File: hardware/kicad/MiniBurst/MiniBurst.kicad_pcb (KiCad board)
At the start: 2 copper layers, 30 x 113.5 mm, 65 parts, among them J1 TRIG_IN, J2 TRIG_OUT, J3 EXT_CLK, J4 DURATION_OUT, J5 END_OUT, J6 PULSES_OUT, J8 Conn_01x10_Pin, SW1 RETRIG, SW2 STEPS, U1 LM358, U2 40106, U3 4017, U4 LM358, U5 LM358

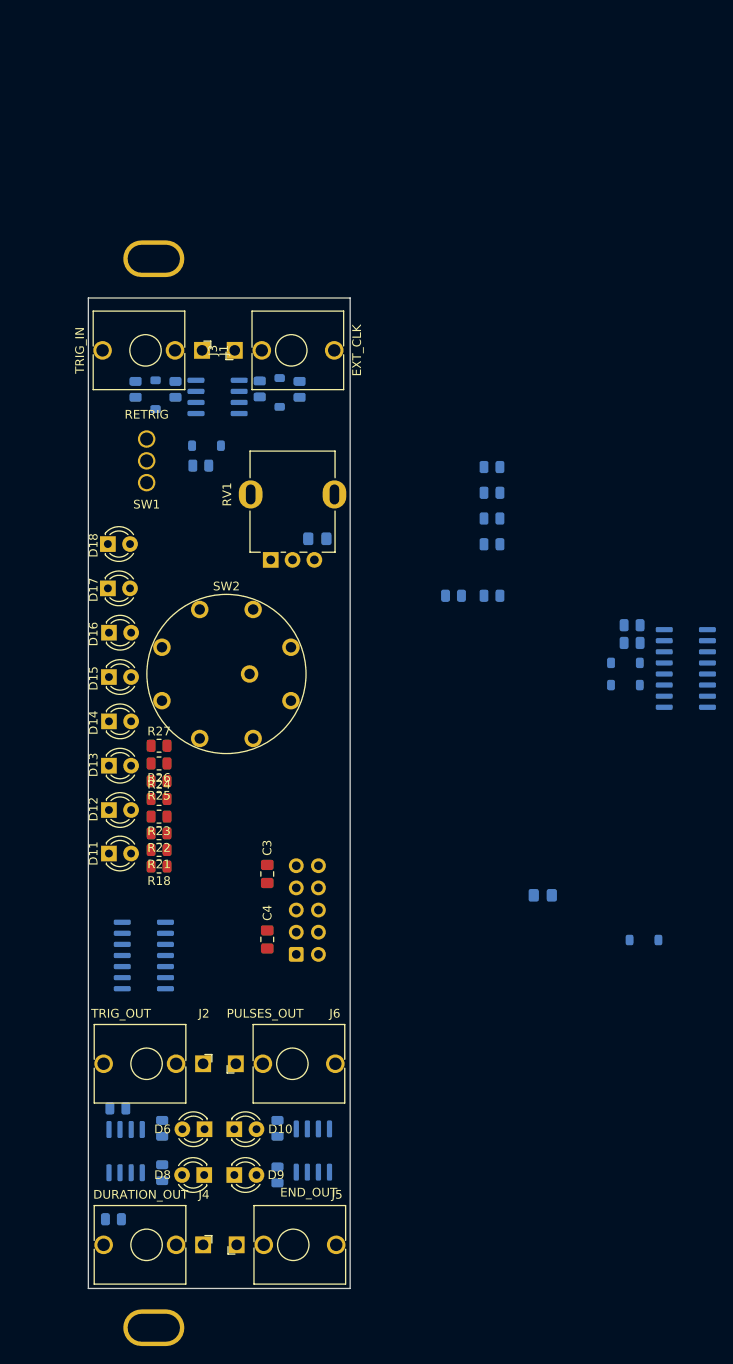
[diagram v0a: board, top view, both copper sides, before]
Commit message: done with panel art
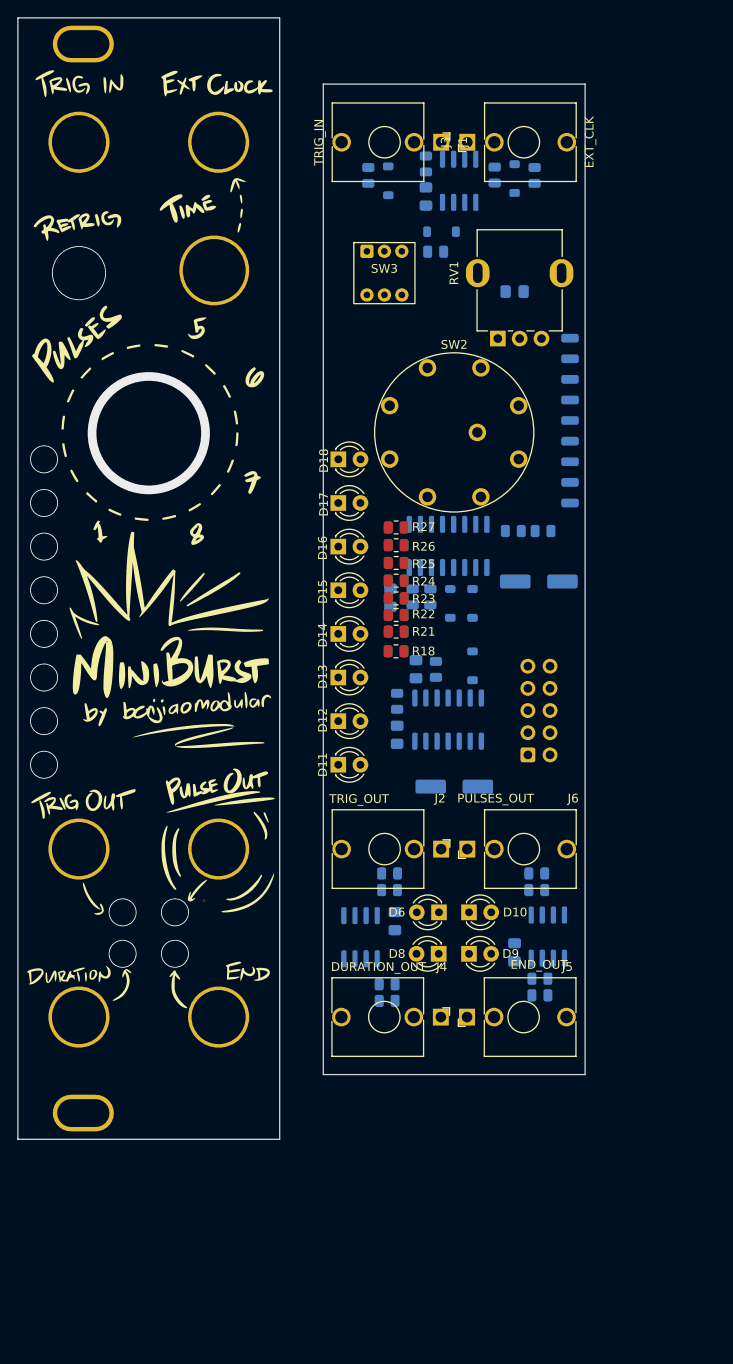
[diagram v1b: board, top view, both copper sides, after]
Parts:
- removed J8: Conn_01x10_Pin, Connector_IDC:IDC-Header_2x05_P2.54mm_Vertical
- removed SW1: RETRIG, benjiaomodular:ToggleSwitch_SMTS-102
- added C5: 100nF, Capacitor_SMD:C_0805_2012Metric_Pad1.18x1.45mm_HandSolder, B.Cu at (138.7, 45.9)
- added C6: 100nF, Capacitor_SMD:C_0805_2012Metric_Pad1.18x1.45mm_HandSolder, B.Cu at (135.1, 128.9)
- added C7: 100nF, Capacitor_SMD:C_0805_2012Metric_Pad1.18x1.45mm_HandSolder, B.Cu at (148.8, 132.5)
- added C8: 100nF, Capacitor_SMD:C_0805_2012Metric_Pad1.18x1.45mm_HandSolder, B.Cu at (134.6, 91.8)
- added C9: 100nF, Capacitor_SMD:C_0805_2012Metric_Pad1.18x1.45mm_HandSolder, B.Cu at (135.4, 107.5)
- added G***: LOGO, LOGO, F.Cu at (107.1, 89.7)
- added J7: Conn_01x10_Pin, Connector_IDC:IDC-Header_2x05_P2.54mm_Vertical, B.Cu at (150.4, 109.9)
- added REF**: PanelHole_AudioJack_3.5mm, benjiaomodular:PanelHole_AudioJack_3.5mm, F.Cu at (108.4, 120.7)
- added REF**: PanelHole_AudioJack_3.5mm, benjiaomodular:PanelHole_AudioJack_3.5mm, F.Cu at (105.4, 139.9)
- added REF**: PanelHole_Potentiometer_RV09, benjiaomodular:PanelHole_Potentiometer_RV09, F.Cu at (111.9, 61.8)
- added REF**: PanelHole_AudioJack_3.5mm, benjiaomodular:PanelHole_AudioJack_3.5mm, F.Cu at (105.4, 120.7)
- added REF**: PanelHole_AudioJack_3.5mm, benjiaomodular:PanelHole_AudioJack_3.5mm, F.Cu at (108.4, 39.6)
- added REF**: PanelHole_AudioJack_3.5mm, benjiaomodular:PanelHole_AudioJack_3.5mm, F.Cu at (108.4, 139.9)
- added REF**: PanelHole_AudioJack_3.5mm, benjiaomodular:PanelHole_AudioJack_3.5mm, F.Cu at (105.4, 39.6)
- added SW3: SW_DPDT_x2, benjiaomodular:Button_KFC7x7, F.Cu at (133.9, 54.6)
- added TP1: TestPoint, Connector_Wire:SolderWirePad_1x01_SMD_1x2mm, B.Cu at (155.2, 81.0)
- added TP2: TestPoint, Connector_Wire:SolderWirePad_1x01_SMD_1x2mm, B.Cu at (155.2, 78.6)
- added TP3: TestPoint, Connector_Wire:SolderWirePad_1x01_SMD_1x2mm, B.Cu at (155.2, 76.3)
- added TP4: TestPoint, Connector_Wire:SolderWirePad_1x01_SMD_1x2mm, B.Cu at (155.2, 73.9)
- added TP5: TestPoint, Connector_Wire:SolderWirePad_1x01_SMD_1x2mm, B.Cu at (155.2, 71.5)
- added TP6: TestPoint, Connector_Wire:SolderWirePad_1x01_SMD_1x2mm, B.Cu at (155.2, 69.2)
- added TP7: TestPoint, Connector_Wire:SolderWirePad_1x01_SMD_1x2mm, B.Cu at (155.2, 66.8)
- added TP8: TestPoint, Connector_Wire:SolderWirePad_1x01_SMD_1x2mm, B.Cu at (155.2, 64.5)
- added TP9: TestPoint, Connector_Wire:SolderWirePad_1x01_SMD_1x2mm, B.Cu at (155.2, 62.1)
- C3, C4: footprint Capacitor_SMD:C_0805_2012Metric_Pad1.18x1.45mm_HandSolder -> Capacitor_SMD:CP_Elec_6.3x4.5; moved to B.Cu
- moved R14 46.9 mm to (151.7, 137.4), turned to 0 degrees
- moved C3 45.7 mm to (151.6, 90.0), turned to 0 degrees
- moved U2 44.1 mm to (141.2, 105.8), turned to -90 degrees
- moved R11 41.2 mm to (134.5, 123.4)
- moved R17 40.4 mm to (151.4, 125.3), turned to 180 degrees
- moved R13 40.1 mm to (134.2, 138.0)
- moved R8 38.6 mm to (138.7, 42.1)
- moved SW2 38.0 mm to (141.9, 72.9)
- moved R15 37.7 mm to (134.5, 125.3), turned to 0 degrees
- moved J4 37.7 mm to (140.4, 139.9)
- moved R20 37.5 mm to (151.7, 135.5), turned to 180 degrees
- moved U1 37.1 mm to (142.5, 44.1), turned to -90 degrees
- moved J5 37.1 mm to (143.4, 139.9)
- moved D5 37.1 mm to (144.0, 99.7), turned to 90 degrees
- moved D9 37.0 mm to (143.6, 132.7)
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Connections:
- J1 pad TN: unconnected-(J1-PadTN) -> Net-(J1-PadTN)
- R6 pad 1: Net-(U5A-+) -> Net-(U4A-+)
- U2 pad 4: Net-(U5A-+) -> Net-(U4A-+)
- U2 pad 5: Net-(U5A-+) -> Net-(U4A-+)
- U4 pad 1: Net-(R17-Pad1) -> Net-(R13-Pad2)
- U4 pad 3: Net-(D2-A) -> Net-(U4A-+)
- U5 pad 1: Net-(R13-Pad2) -> Net-(R17-Pad1)
- U5 pad 3: Net-(U5A-+) -> Net-(D2-A)
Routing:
- net (no net): vias 0 -> 14
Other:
- board size 30 x 113.5 mm -> 65 x 128.5 mm
